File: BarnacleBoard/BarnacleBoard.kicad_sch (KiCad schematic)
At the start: 101 parts, among them J1 Conn_02x35_Top_Bottom, J11 Connector_Breadboard

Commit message: started routing
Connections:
- net at JP1.2 (B), TP15.1, TP15.1: now also J1.61 (Pin_61), J11.61 (Top_Pos); no longer J1.62 (Pin_62), J11.62 (Top_Neg)
- net at JP2.1 (A), TP15.1, TP15.1: now also J1.62 (Pin_62), J11.62 (Top_Neg); no longer J1.61 (Pin_61), J11.61 (Top_Pos)

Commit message: Messing around with a new version using the 5-hole spring clips
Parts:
- removed D1: WS2812B, JumperlessFootprints:LED_WS2812B-2020_PLCC4_2.0x2.0mm, symbol JumperlessSymbols:WS2812B_13
- removed D10: WS2812B, JumperlessFootprints:LED_WS2812B-2020_PLCC4_2.0x2.0mm, symbol JumperlessSymbols:WS2812B_45
- removed D11: WS2812B, JumperlessFootprints:LED_WS2812B-2020_PLCC4_2.0x2.0mm, symbol JumperlessSymbols:WS2812B_14
- removed D12: WS2812B, JumperlessFootprints:LED_WS2812B-2020_PLCC4_2.0x2.0mm, symbol JumperlessSymbols:WS2812B_47
- removed D13: WS2812B, JumperlessFootprints:LED_WS2812B-2020_PLCC4_2.0x2.0mm, symbol JumperlessSymbols:WS2812B_40
- removed D14: WS2812B, JumperlessFootprints:LED_WS2812B-2020_PLCC4_2.0x2.0mm, symbol JumperlessSymbols:WS2812B_44
- removed D15: WS2812B, JumperlessFootprints:LED_WS2812B-2020_PLCC4_2.0x2.0mm, symbol JumperlessSymbols:WS2812B_43
- removed D16: WS2812B, JumperlessFootprints:LED_WS2812B-2020_PLCC4_2.0x2.0mm, symbol JumperlessSymbols:WS2812B_25
- removed D17: WS2812B, JumperlessFootprints:LED_WS2812B-2020_PLCC4_2.0x2.0mm, symbol JumperlessSymbols:WS2812B_28
- removed D18: WS2812B, JumperlessFootprints:LED_WS2812B-2020_PLCC4_2.0x2.0mm, symbol JumperlessSymbols:WS2812B_27
- removed D19: WS2812B, JumperlessFootprints:LED_WS2812B-2020_PLCC4_2.0x2.0mm, symbol JumperlessSymbols:WS2812B_30
- removed D2: WS2812B, JumperlessFootprints:LED_WS2812B-2020_PLCC4_2.0x2.0mm, symbol JumperlessSymbols:WS2812B_36
- removed D20: WS2812B, JumperlessFootprints:LED_WS2812B-2020_PLCC4_2.0x2.0mm, symbol JumperlessSymbols:WS2812B_29
- removed D21: WS2812B, JumperlessFootprints:LED_WS2812B-2020_PLCC4_2.0x2.0mm, symbol JumperlessSymbols:WS2812B_26
- removed D22: WS2812B, JumperlessFootprints:LED_WS2812B-2020_PLCC4_2.0x2.0mm, symbol JumperlessSymbols:WS2812B_12
- removed D23: WS2812B, JumperlessFootprints:LED_WS2812B-2020_PLCC4_2.0x2.0mm, symbol JumperlessSymbols:WS2812B_31
- removed D24: WS2812B, JumperlessFootprints:LED_WS2812B-2020_PLCC4_2.0x2.0mm, symbol JumperlessSymbols:WS2812B_34
- removed D25: WS2812B, JumperlessFootprints:LED_WS2812B-2020_PLCC4_2.0x2.0mm, symbol JumperlessSymbols:WS2812B_35
- removed D26: WS2812B, JumperlessFootprints:LED_WS2812B-2020_PLCC4_2.0x2.0mm, symbol JumperlessSymbols:WS2812B_16
- removed D27: WS2812B, JumperlessFootprints:LED_WS2812B-2020_PLCC4_2.0x2.0mm, symbol JumperlessSymbols:WS2812B_20
- removed D28: WS2812B, JumperlessFootprints:LED_WS2812B-2020_PLCC4_2.0x2.0mm, symbol JumperlessSymbols:WS2812B_21
- removed D29: WS2812B, JumperlessFootprints:LED_WS2812B-2020_PLCC4_2.0x2.0mm, symbol JumperlessSymbols:WS2812B_24
- removed D3: WS2812B, JumperlessFootprints:LED_WS2812B-2020_PLCC4_2.0x2.0mm, symbol JumperlessSymbols:WS2812B_37
- removed D30: WS2812B, JumperlessFootprints:LED_WS2812B-2020_PLCC4_2.0x2.0mm, symbol JumperlessSymbols:WS2812B_19
- removed D31: WS2812B, JumperlessFootprints:LED_WS2812B-2020_PLCC4_2.0x2.0mm, symbol JumperlessSymbols:WS2812B_67
- removed D32: WS2812B, JumperlessFootprints:LED_WS2812B-2020_PLCC4_2.0x2.0mm, symbol JumperlessSymbols:WS2812B_66
- removed D33: WS2812B, JumperlessFootprints:LED_WS2812B-2020_PLCC4_2.0x2.0mm, symbol JumperlessSymbols:WS2812B_65
- removed D34: WS2812B, JumperlessFootprints:LED_WS2812B-2020_PLCC4_2.0x2.0mm, symbol JumperlessSymbols:WS2812B_70
- removed D35: WS2812B, JumperlessFootprints:LED_WS2812B-2020_PLCC4_2.0x2.0mm, symbol JumperlessSymbols:WS2812B_69
- removed D36: WS2812B, JumperlessFootprints:LED_WS2812B-2020_PLCC4_2.0x2.0mm, symbol JumperlessSymbols:WS2812B_68
- removed D37: WS2812B, JumperlessFootprints:LED_WS2812B-2020_PLCC4_2.0x2.0mm, symbol JumperlessSymbols:WS2812B_3
- removed D38: WS2812B, JumperlessFootprints:LED_WS2812B-2020_PLCC4_2.0x2.0mm, symbol JumperlessSymbols:WS2812B_4
- removed D39: WS2812B, JumperlessFootprints:LED_WS2812B-2020_PLCC4_2.0x2.0mm, symbol JumperlessSymbols:WS2812B_6
- removed D4: WS2812B, JumperlessFootprints:LED_WS2812B-2020_PLCC4_2.0x2.0mm, symbol JumperlessSymbols:WS2812B_39
- removed D40: WS2812B, JumperlessFootprints:LED_WS2812B-2020_PLCC4_2.0x2.0mm, symbol JumperlessSymbols:WS2812B_5
- removed D41: WS2812B, JumperlessFootprints:LED_WS2812B-2020_PLCC4_2.0x2.0mm, symbol JumperlessSymbols:WS2812B_8
- removed D42: WS2812B, JumperlessFootprints:LED_WS2812B-2020_PLCC4_2.0x2.0mm, symbol JumperlessSymbols:WS2812B_10
- removed D43: WS2812B, JumperlessFootprints:LED_WS2812B-2020_PLCC4_2.0x2.0mm, symbol JumperlessSymbols:WS2812B_9
- removed D44: WS2812B, JumperlessFootprints:LED_WS2812B-2020_PLCC4_2.0x2.0mm, symbol JumperlessSymbols:WS2812B_2
- removed D45: WS2812B, JumperlessFootprints:LED_WS2812B-2020_PLCC4_2.0x2.0mm, symbol JumperlessSymbols:WS2812B_1
- removed D46: WS2812B, JumperlessFootprints:LED_WS2812B-2020_PLCC4_2.0x2.0mm, symbol JumperlessSymbols:WS2812B_11
- removed D47: WS2812B, JumperlessFootprints:LED_WS2812B-2020_PLCC4_2.0x2.0mm, symbol JumperlessSymbols:WS2812B_49
- removed D48: WS2812B, JumperlessFootprints:LED_WS2812B-2020_PLCC4_2.0x2.0mm, symbol JumperlessSymbols:WS2812B_48
- removed D49: WS2812B, JumperlessFootprints:LED_WS2812B-2020_PLCC4_2.0x2.0mm, symbol JumperlessSymbols:WS2812B_50
- removed D5: WS2812B, JumperlessFootprints:LED_WS2812B-2020_PLCC4_2.0x2.0mm, symbol JumperlessSymbols:WS2812B_38
- removed D50: WS2812B, JumperlessFootprints:LED_WS2812B-2020_PLCC4_2.0x2.0mm, symbol JumperlessSymbols:WS2812B_51
- removed D51: WS2812B, JumperlessFootprints:LED_WS2812B-2020_PLCC4_2.0x2.0mm, symbol JumperlessSymbols:WS2812B_52
- removed D52: WS2812B, JumperlessFootprints:LED_WS2812B-2020_PLCC4_2.0x2.0mm, symbol JumperlessSymbols:WS2812B_53
- removed D53: WS2812B, JumperlessFootprints:LED_WS2812B-2020_PLCC4_2.0x2.0mm, symbol JumperlessSymbols:WS2812B_54
- removed D54: WS2812B, JumperlessFootprints:LED_WS2812B-2020_PLCC4_2.0x2.0mm, symbol JumperlessSymbols:WS2812B_55
- removed D55: WS2812B, JumperlessFootprints:LED_WS2812B-2020_PLCC4_2.0x2.0mm, symbol JumperlessSymbols:WS2812B_33
- removed D56: WS2812B, JumperlessFootprints:LED_WS2812B-2020_PLCC4_2.0x2.0mm, symbol JumperlessSymbols:WS2812B_32
- removed D57: WS2812B, JumperlessFootprints:LED_WS2812B-2020_PLCC4_2.0x2.0mm, symbol JumperlessSymbols:WS2812B_22
- removed D58: WS2812B, JumperlessFootprints:LED_WS2812B-2020_PLCC4_2.0x2.0mm, symbol JumperlessSymbols:WS2812B_17
- removed D59: WS2812B, JumperlessFootprints:LED_WS2812B-2020_PLCC4_2.0x2.0mm, symbol JumperlessSymbols:WS2812B_23
- removed D6: WS2812B, JumperlessFootprints:LED_WS2812B-2020_PLCC4_2.0x2.0mm, symbol JumperlessSymbols:WS2812B_15
- removed D60: WS2812B, JumperlessFootprints:LED_WS2812B-2020_PLCC4_2.0x2.0mm, symbol JumperlessSymbols:WS2812B_18
- removed D7: WS2812B, JumperlessFootprints:LED_WS2812B-2020_PLCC4_2.0x2.0mm, symbol JumperlessSymbols:WS2812B_42
- removed D71: WS2812B, JumperlessFootprints:LED_WS2812B-2020_PLCC4_2.0x2.0mm, symbol JumperlessSymbols:WS2812B_78
- removed D72: WS2812B, JumperlessFootprints:LED_WS2812B-2020_PLCC4_2.0x2.0mm, symbol JumperlessSymbols:WS2812B_79
- removed D73: WS2812B, JumperlessFootprints:LED_WS2812B-2020_PLCC4_2.0x2.0mm, symbol JumperlessSymbols:WS2812B
- removed D74: WS2812B, JumperlessFootprints:LED_WS2812B-2020_PLCC4_2.0x2.0mm, symbol JumperlessSymbols:WS2812B_75
- removed D75: WS2812B, JumperlessFootprints:LED_WS2812B-2020_PLCC4_2.0x2.0mm, symbol JumperlessSymbols:WS2812B_74
- removed D76: WS2812B, JumperlessFootprints:LED_WS2812B-2020_PLCC4_2.0x2.0mm, symbol JumperlessSymbols:WS2812B_76
- removed D77: WS2812B, JumperlessFootprints:LED_WS2812B-2020_PLCC4_2.0x2.0mm, symbol JumperlessSymbols:WS2812B_77
- removed D78: WS2812B, JumperlessFootprints:LED_WS2812B-2020_PLCC4_2.0x2.0mm, symbol JumperlessSymbols:WS2812B_72
- removed D79: WS2812B, JumperlessFootprints:LED_WS2812B-2020_PLCC4_2.0x2.0mm, symbol JumperlessSymbols:WS2812B_73
- removed D8: WS2812B, JumperlessFootprints:LED_WS2812B-2020_PLCC4_2.0x2.0mm, symbol JumperlessSymbols:WS2812B_41
- removed D80: WS2812B, JumperlessFootprints:LED_WS2812B-2020_PLCC4_2.0x2.0mm, symbol JumperlessSymbols:WS2812B_71
- removed D81: WS2812B, JumperlessFootprints:LED_WS2812B-2020_PLCC4_2.0x2.0mm, symbol JumperlessSymbols:WS2812B_61
- removed D82: WS2812B, JumperlessFootprints:LED_WS2812B-2020_PLCC4_2.0x2.0mm, symbol JumperlessSymbols:WS2812B_63
- removed D83: WS2812B, JumperlessFootprints:LED_WS2812B-2020_PLCC4_2.0x2.0mm, symbol JumperlessSymbols:WS2812B_62
- removed D84: WS2812B, JumperlessFootprints:LED_WS2812B-2020_PLCC4_2.0x2.0mm, symbol JumperlessSymbols:WS2812B_64
- removed D85: WS2812B, JumperlessFootprints:LED_WS2812B-2020_PLCC4_2.0x2.0mm, symbol JumperlessSymbols:WS2812B_60
- removed D86: WS2812B, JumperlessFootprints:LED_WS2812B-2020_PLCC4_2.0x2.0mm, symbol JumperlessSymbols:WS2812B_56
- removed D87: WS2812B, JumperlessFootprints:LED_WS2812B-2020_PLCC4_2.0x2.0mm, symbol JumperlessSymbols:WS2812B_59
- removed D88: WS2812B, JumperlessFootprints:LED_WS2812B-2020_PLCC4_2.0x2.0mm, symbol JumperlessSymbols:WS2812B_58
- removed D89: WS2812B, JumperlessFootprints:LED_WS2812B-2020_PLCC4_2.0x2.0mm, symbol JumperlessSymbols:WS2812B_57
- removed D9: WS2812B, JumperlessFootprints:LED_WS2812B-2020_PLCC4_2.0x2.0mm, symbol JumperlessSymbols:WS2812B_46
- removed D90: WS2812B, JumperlessFootprints:LED_WS2812B-2020_PLCC4_2.0x2.0mm, symbol JumperlessSymbols:WS2812B_7
- removed TP15: LED DOUT, Connector_PinHeader_2.54mm:PinHeader_1x01_P2.54mm_Vertical_Rounded, symbol JumperlessSymbols:TestPoint
- renumbered TP15 to TP16, TP15 to TP17, TP15 to TP18, TP15 to TP19, TP15 to TP20, TP15 to TP21, TP15 to TP22, TP15 to TP23, TP15 to TP24, TP15 to TP25, TP15 to TP26, TP15 to TP27, TP15 to TP28, TP15 to TP29, TP15 to TP30, TP15 to TP31
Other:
- added sheet LEDs (JustTheLEDs.kicad_sch)
- note added: "All the LEDs are down here"
- note removed: "Breadboard LEDS (this will actually be on a separate flex PCB so it can fit inside the breadboard)"
- moved on the sheet: TP16, TP17, TP18, TP19, TP20, TP21, TP22, TP23

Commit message: The future is happening
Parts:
- added J10, J7: Conn_01x03, symbol Connector_Generic:Conn_01x03
- added unit 2 of J11
- added J12: Conn_02x03_Top_Bottom, JumperlessFootprints:SideConnect_short_right, symbol Connector_Generic:Conn_02x03_Top_Bottom
- added J13: Conn_02x03_Top_Bottom, JumperlessFootprints:SideConnect_short_left, symbol Connector_Generic:Conn_02x03_Top_Bottom
- added J14: Conn_01x06, JumperlessFootprints:GT-B0353FSV06-02B0201, symbol Connector_Generic:Conn_01x06
- added J15: Conn_01x01, JumperlessFootprints:PinHeader_1x1_Smaller, symbol Connector_Generic:Conn_01x01
- added J2: pad_sense_1, JumperlessFootprints:PinHeader_1x1_Smaller, symbol Connector:Conn_01x01_Pin
- added J3: pad_sense_30, JumperlessFootprints:PinHeader_1x1_Smaller, symbol Connector:Conn_01x01_Pin
- added J4: pad_sense_60, JumperlessFootprints:PinHeader_1x1_Smaller, symbol Connector:Conn_01x01_Pin
- added J5: pad_sense_31, JumperlessFootprints:PinHeader_1x1_Smaller, symbol Connector:Conn_01x01_Pin
- added J6: Conn_02x35_Top_Bottom, JumperlessFootprints:SideConnect_sparserrr_Bottom, symbol Connector_Generic:Conn_02x35_JumperluxCardEdge
- added J8: J8, symbol JumperlessSymbols:SideConnect
- added J9: RIGHT, symbol JumperlessSymbols:SideConnect
- added JP10, JP3, JP4, JP5, JP6, JP7, JP8, JP9: SolderJumper_2_Open, JumperlessFootprints:SolderJumper_2_Open_Small, symbol Jumper:SolderJumper_2_Open
- J11: symbol JumperlessSymbols:Breadboard_correctPins -> JumperlessSymbols:Breadboard_BBunits
- TP16, TP20, TP21, TP22, TP23, TP25, TP27, TP29, TP31: footprint Connector_PinHeader_2.54mm:PinHeader_1x01_P2.54mm_Vertical_Rounded -> JumperlessFootprints:PINHEADER_Larger_Pad
- TP17, TP18, TP19: footprint Connector_PinHeader_2.54mm:PinHeader_1x01_P2.54mm_Vertical_Rounded -> JumperlessFootprints:TestPoint_D0.75mm
- TP28, TP30: footprint Connector_PinHeader_2.54mm:PinHeader_1x01_P2.54mm_Vertical_Rounded -> JumperlessFootprints:PINHEADER-1x1_vertical
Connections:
- net +5V: now also J14.3 (Pin_3), J14.6 (Pin_6), J6.70 (Pin_70), J7.1 (Pin_1); no longer J1.67 (Pin_67)
- net GND: now also J14.4 (Pin_4), J14.5 (Pin_5), J6.68 (Pin_68), J7.3 (Pin_3); no longer J1.65 (Pin_65)
- net LED_IN: now also J14.1 (Pin_1), J14.2 (Pin_2), J6.69 (Pin_69), J7.2 (Pin_2)
- net LED_OUT: no longer J1.66 (Pin_66)
- net BOT_POS: now reaches J1.63 (Pin_63), J11.63 (Bot_Pos), JP1.1 (A), TP28.1, TP29.1
- net BOT_POS: now also J6.63 (Pin_63), JP5.2 (B), JP9.2 (B)
- net TOP_POS: now reaches J1.61 (Pin_61), J11.61 (Top_Pos), JP1.2 (B), TP24.1, TP25.1
- net TOP_POS: now also J6.61 (Pin_61), JP3.2 (B), JP7.2 (B)
- net TOP_NEG: now reaches J1.62 (Pin_62), J11.62 (Top_Neg), JP2.1 (A), TP26.1, TP27.1
- net TOP_NEG: now also J6.62 (Pin_62), JP10.1 (A), JP6.1 (A)
- net BOT_NEG: now reaches J1.64 (Pin_64), J11.64 (Bot_Neg), JP2.2 (B), TP30.1, TP31.1
- net BOT_NEG: now also J6.64 (Pin_64), JP4.2 (B), JP8.2 (B)
- net at J1.1 (Pin_1), J11.1 (Pin_1): now also J6.1 (Pin_1)
- net at J1.10 (Pin_10), J11.10 (Pin_10): now also J6.10 (Pin_10)
- net at J1.11 (Pin_11), J11.11 (Pin_11): now also J6.11 (Pin_11)
- net at J1.12 (Pin_12), J11.12 (Pin_12): now also J6.12 (Pin_12)
- net at J1.13 (Pin_13), J11.13 (Pin_13): now also J6.13 (Pin_13)
- net at J1.14 (Pin_14), J11.14 (Pin_14): now also J6.14 (Pin_14)
- net at J1.15 (Pin_15), J11.15 (Pin_15): now also J6.15 (Pin_15)
- net at J1.16 (Pin_16), J11.16 (Pin_16): now also J6.16 (Pin_16)
- net at J1.17 (Pin_17), J11.17 (Pin_17): now also J6.17 (Pin_17)
- net at J1.18 (Pin_18), J11.18 (Pin_18): now also J6.18 (Pin_18)
- net at J1.19 (Pin_19), J11.19 (Pin_19): now also J6.19 (Pin_19)
- net at J1.2 (Pin_2), J11.2 (Pin_2): now also J6.2 (Pin_2)
- net at J1.20 (Pin_20), J11.20 (Pin_20): now also J6.20 (Pin_20)
- net at J1.21 (Pin_21), J11.21 (Pin_21): now also J6.21 (Pin_21)
- net at J1.22 (Pin_22), J11.22 (Pin_22): now also J6.22 (Pin_22)
- net at J1.23 (Pin_23), J11.23 (Pin_23): now also J6.23 (Pin_23)
- net at J1.24 (Pin_24), J11.24 (Pin_24): now also J6.24 (Pin_24)
- net at J1.25 (Pin_25), J11.25 (Pin_25): now also J6.25 (Pin_25)
- net at J1.26 (Pin_26), J11.26 (Pin_26): now also J6.26 (Pin_26)
- net at J1.27 (Pin_27), J11.27 (Pin_27): now also J6.27 (Pin_27)
- net at J1.28 (Pin_28), J11.28 (Pin_28): now also J6.28 (Pin_28)
- net at J1.29 (Pin_29), J11.29 (Pin_29): now also J6.29 (Pin_29)
- net at J1.3 (Pin_3), J11.3 (Pin_3): now also J6.3 (Pin_3)
- net at J1.30 (Pin_30), J11.30 (Pin_30): now also J6.30 (Pin_30)
- net at J1.31 (Pin_31), J11.31 (Pin_31): now also J6.31 (Pin_31)
- net at J1.32 (Pin_32), J11.32 (Pin_0): now also J6.32 (Pin_32)
- net at J1.33 (Pin_33), J11.33 (Pin_1): now also J6.33 (Pin_33)
- net at J1.34 (Pin_34), J11.34 (Pin_2): now also J6.34 (Pin_34)
- net at J1.35 (Pin_35), J11.35 (Pin_3): now also J6.35 (Pin_35)
- net at J1.36 (Pin_36), J11.36 (Pin_4): now also J6.36 (Pin_36)
- net at J1.37 (Pin_37), J11.37 (Pin_5): now also J6.37 (Pin_37)
- net at J1.38 (Pin_38), J11.38 (Pin_6): now also J6.38 (Pin_38)
- net at J1.39 (Pin_39), J11.39 (Pin_7): now also J6.39 (Pin_39)
- net at J1.4 (Pin_4), J11.4 (Pin_4): now also J6.4 (Pin_4)
- net at J1.40 (Pin_40), J11.40 (Pin_8): now also J6.40 (Pin_40)
- net at J1.41 (Pin_41), J11.41 (Pin_9): now also J6.41 (Pin_41)
- net at J1.42 (Pin_42), J11.42 (Pin_10): now also J6.42 (Pin_42)
- net at J1.43 (Pin_43), J11.43 (Pin_11): now also J6.43 (Pin_43)
- net at J1.44 (Pin_44), J11.44 (Pin_12): now also J6.44 (Pin_44)
- net at J1.45 (Pin_45), J11.45 (Pin_13): now also J6.45 (Pin_45)
- net at J1.46 (Pin_46), J11.46 (Pin_14): now also J6.46 (Pin_46)
- net at J1.47 (Pin_47), J11.47 (Pin_15): now also J6.47 (Pin_47)
- net at J1.48 (Pin_48), J11.48 (Pin_16): now also J6.48 (Pin_48)
- net at J1.49 (Pin_49), J11.49 (Pin_17): now also J6.49 (Pin_49)
- net at J1.5 (Pin_5), J11.5 (Pin_5): now also J6.5 (Pin_5)
- net at J1.50 (Pin_50), J11.50 (Pin_18): now also J6.50 (Pin_50)
- net at J1.51 (Pin_51), J11.51 (Pin_19): now also J6.51 (Pin_51)
- net at J1.52 (Pin_52), J11.52 (Pin_20): now also J6.52 (Pin_52)
- net at J1.53 (Pin_53), J11.53 (Pin_21): now also J6.53 (Pin_53)
- net at J1.54 (Pin_54), J11.54 (Pin_22): now also J6.54 (Pin_54)
- net at J1.55 (Pin_55), J11.55 (Pin_23): now also J6.55 (Pin_55)
- net at J1.56 (Pin_56), J11.56 (Pin_24): now also J6.56 (Pin_56)
- net at J1.57 (Pin_57), J11.57 (Pin_25): now also J6.57 (Pin_57)
- net at J1.58 (Pin_58), J11.58 (Pin_26): now also J6.58 (Pin_58)
- net at J1.59 (Pin_59), J11.59 (Pin_27): now also J6.59 (Pin_59)
- net at J1.6 (Pin_6), J11.6 (Pin_6): now also J6.6 (Pin_6)
- net at J1.60 (Pin_60), J11.60 (Pin_28): now also J6.60 (Pin_60)
- net at J1.7 (Pin_7), J11.7 (Pin_7): now also J6.7 (Pin_7)
- net at J1.8 (Pin_8), J11.8 (Pin_8): now also J6.8 (Pin_8)
- net at J1.9 (Pin_9), J11.9 (Pin_9): now also J6.9 (Pin_9)
- new net: J12.5 (Pin_5), JP8.1 (A)
- new net: J1.65 (Pin_65), J15.1 (Pin_1), J6.65 (Pin_65)
- new net: J3.1 (Pin_1), J5.1 (Pin_1)
- new net: J11.5 (Pin_5), J8.B10 (Pin_40)
- new net: J11.6 (Pin_6), J8.B12 (Pin_42)
- new net: J11.7 (Pin_7), J8.B14 (Pin_44)
- new net: J11.8 (Pin_8), J8.B16 (Pin_46)
- new net: J11.9 (Pin_9), J8.B18 (Pin_48)
- new net: J11.1 (Pin_1), J8.B2 (Pin_32)
- new net: J11.10 (Pin_10), J8.B20 (Pin_50)
- new net: J11.11 (Pin_11), J8.B22 (Pin_52)
- new net: J11.12 (Pin_12), J8.B24 (Pin_54)
- new net: J11.13 (Pin_13), J8.B26 (Pin_56)
- new net: J11.14 (Pin_14), J8.B28 (Pin_58)
- new net: J11.15 (Pin_15), J8.B30 (Pin_60)
- new net: J11.31 (Pin_31), J8.B32 (Pin_32)
- new net: J11.32 (Pin_0), J8.B34 (Pin_34)
- new net: J11.33 (Pin_1), J8.B36 (Pin_36)
- new net: J11.34 (Pin_2), J8.B38 (Pin_38)
- new net: J11.2 (Pin_2), J8.B4 (Pin_34)
- new net: J11.35 (Pin_3), J8.B40 (Pin_40)
- new net: J11.36 (Pin_4), J8.B42 (Pin_42)
- new net: J11.37 (Pin_5), J8.B44 (Pin_44)
- new net: J11.38 (Pin_6), J8.B46 (Pin_46)
- new net: J11.39 (Pin_7), J8.B48 (Pin_48)
- new net: J11.40 (Pin_8), J8.B50 (Pin_50)
- new net: J11.41 (Pin_9), J8.B52 (Pin_52)
- new net: J11.42 (Pin_10), J8.B54 (Pin_54)
- new net: J11.43 (Pin_11), J8.B56 (Pin_56)
- new net: J11.44 (Pin_12), J8.B58 (Pin_58)
- new net: J11.3 (Pin_3), J8.B6 (Pin_36)
- new net: J11.45 (Pin_13), J8.B60 (Pin_60)
- new net: J11.4 (Pin_4), J8.B8 (Pin_38)
- new net: J12.3 (Pin_3), J12.6 (Pin_6), JP9.1 (A)
- new net: J13.3 (Pin_3), J13.6 (Pin_6), JP5.1 (A)
- new net: J12.1 (Pin_1), J12.4 (Pin_4), JP7.1 (A)
- new net: J12.2 (Pin_2), JP10.2 (B)
- new net: J13.1 (Pin_1), J13.4 (Pin_4), JP3.1 (A)
- new net: J13.2 (Pin_2), JP6.2 (B)
- new net: J13.5 (Pin_5), JP4.1 (A)
- new net: J11.16 (Pin_16), J9.B1 (Pin_31)
- new net: J11.21 (Pin_21), J9.B11 (Pin_41)
- new net: J11.22 (Pin_22), J9.B13 (Pin_43)
- new net: J11.23 (Pin_23), J9.B15 (Pin_45)
- new net: J11.24 (Pin_24), J9.B17 (Pin_47)
- new net: J11.25 (Pin_25), J9.B19 (Pin_49)
- new net: J11.26 (Pin_26), J9.B21 (Pin_51)
- new net: J11.27 (Pin_27), J9.B23 (Pin_53)
- new net: J11.28 (Pin_28), J9.B25 (Pin_55)
- new net: J11.29 (Pin_29), J9.B27 (Pin_57)
- new net: J11.30 (Pin_30), J9.B29 (Pin_59)
- new net: J11.17 (Pin_17), J9.B3 (Pin_33)
- new net: J11.46 (Pin_14), J9.B31 (Pin_31)
- new net: J11.47 (Pin_15), J9.B33 (Pin_33)
- new net: J11.48 (Pin_16), J9.B35 (Pin_35)
- new net: J11.49 (Pin_17), J9.B37 (Pin_37)
- new net: J11.50 (Pin_18), J9.B39 (Pin_39)
- new net: J11.51 (Pin_19), J9.B41 (Pin_41)
- new net: J11.52 (Pin_20), J9.B43 (Pin_43)
- new net: J11.53 (Pin_21), J9.B45 (Pin_45)
- new net: J11.54 (Pin_22), J9.B47 (Pin_47)
- new net: J11.55 (Pin_23), J9.B49 (Pin_49)
- new net: J11.18 (Pin_18), J9.B5 (Pin_35)
- new net: J11.56 (Pin_24), J9.B51 (Pin_51)
- new net: J11.57 (Pin_25), J9.B53 (Pin_53)
- new net: J11.58 (Pin_26), J9.B55 (Pin_55)
- new net: J11.59 (Pin_27), J9.B57 (Pin_57)
- new net: J11.60 (Pin_28), J9.B59 (Pin_59)
- new net: J11.19 (Pin_19), J9.B7 (Pin_37)
- new net: J11.20 (Pin_20), J9.B9 (Pin_39)
- new net PAD_SENSE_IN: J1.66 (Pin_66), J2.1 (Pin_1), J6.66 (Pin_66)
- new net PAD_SENSE_OUT: J1.67 (Pin_67), J4.1 (Pin_1), J6.67 (Pin_67)
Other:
- moved on the sheet: J1, J11A, TP24, TP25, TP26, TP27, TP28, TP29, TP30, TP31

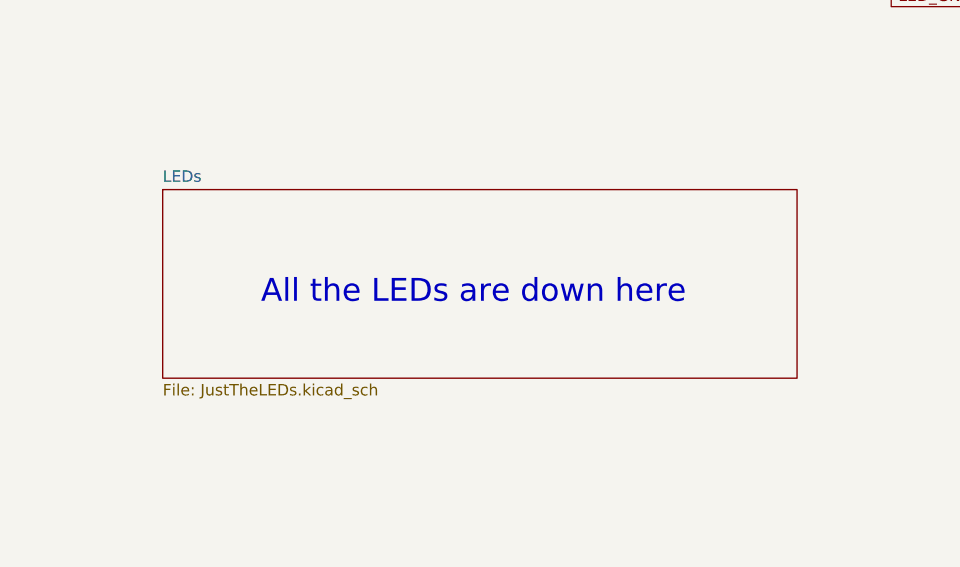
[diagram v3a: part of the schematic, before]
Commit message: actually route most of the barnacles
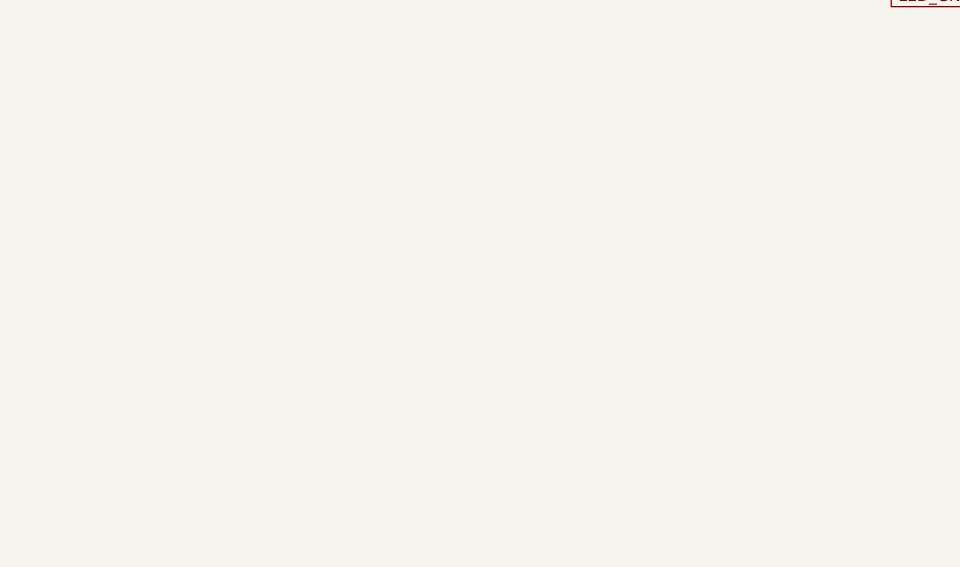
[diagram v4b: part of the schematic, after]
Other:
- removed sheet LEDs
- note removed: "All the LEDs are down here"
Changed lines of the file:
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@@
 	(generator_version "9.0")
 	(paper "A1")
-	(text "All the LEDs are down here"
-		(exclude_from_sim no)
-		(at 72.644 105.41 0)
-		(effects
-			(font
-				(size 2.54 2.54)
-			)
-		)
-	)
 	(junction
 		(at 27.94 34.29)
@@
 				)
 			)
-		)
-	)
-	(sheet
-		(at 38.1 93.98)
-		(size 70.485 20.955)
-		(exclude_from_sim yes)
-		(in_bom no)
-		(on_board no)
-		(dnp yes)
-		(fields_autoplaced yes)
-		(stroke
-			(width 0.1524)
-			(type solid)
-		)
-		(fill
-			(color 0 0 0 0.0000)
-		)
-		(property "Sheetname" "LEDs"
-			(at 38.1 93.2684 0)
-			(effects
-				(font
-					(size 1.27 1.27)
-				)
-				(justify left bottom)
-			)
-		)
-		(property "Sheetfile" "JustTheLEDs.kicad_sch"
-			(at 38.1 115.5196 0)
-			(effects
-				(font
-					(size 1.27 1.27)
-				)
-				(justify left top)
-			)
-		)
-		(instances
-			(project "BarnacleBoard"
-				(path "/9d20a3da-9ae0-4d82-a466-4a6a36bdc64c"
-					(page "2")
-				)
-			)
